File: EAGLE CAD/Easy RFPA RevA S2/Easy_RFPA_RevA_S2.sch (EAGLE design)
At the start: 197 parts, among them J101 COAX112640BNC_EDGE, J102 COAX112640BNC_EDGE, J301 COAX112640BNC_EDGE, J302 COAX112640BNC_EDGE, J401 HDR_2X1282836-1282836-1, J402 KK_PCFAN, Q101 IRF520N, Q102 IRF630, Q201 IRF630, Q202 IRF630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

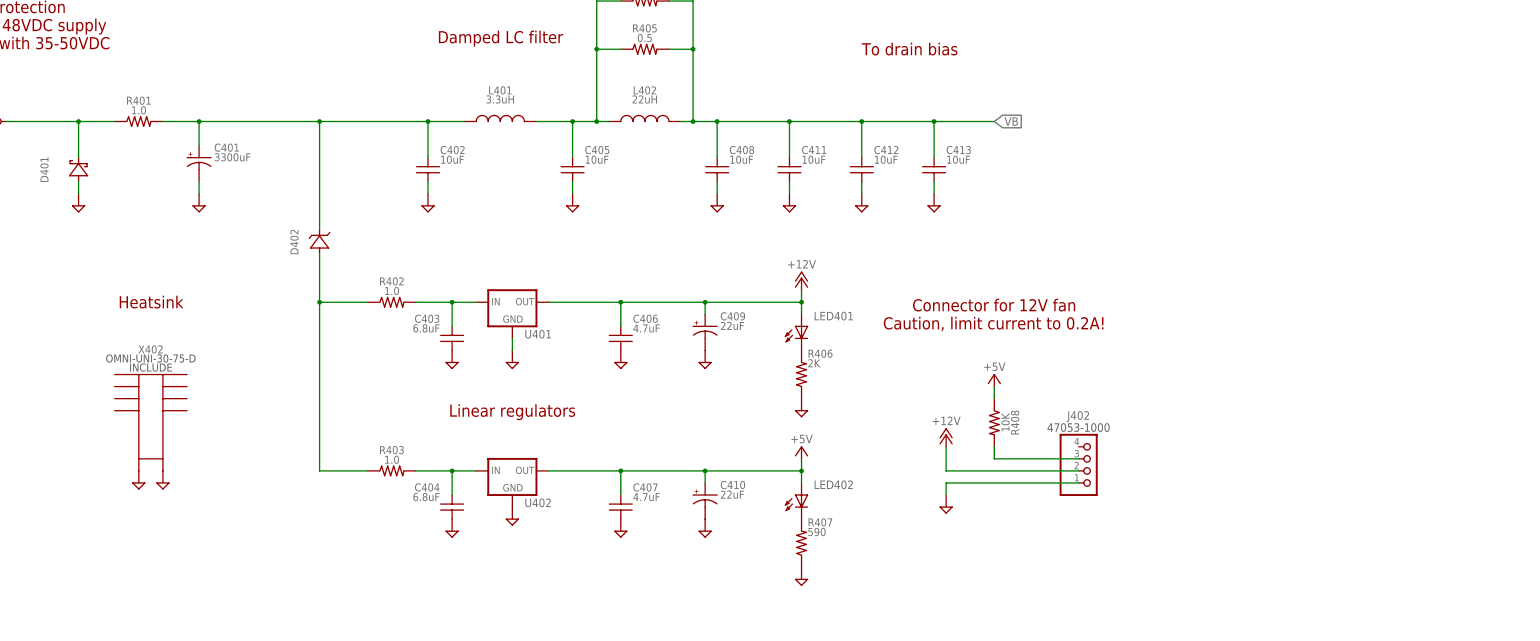
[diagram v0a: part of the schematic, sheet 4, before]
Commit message: Copy the pads and clips to revA S1 and S2
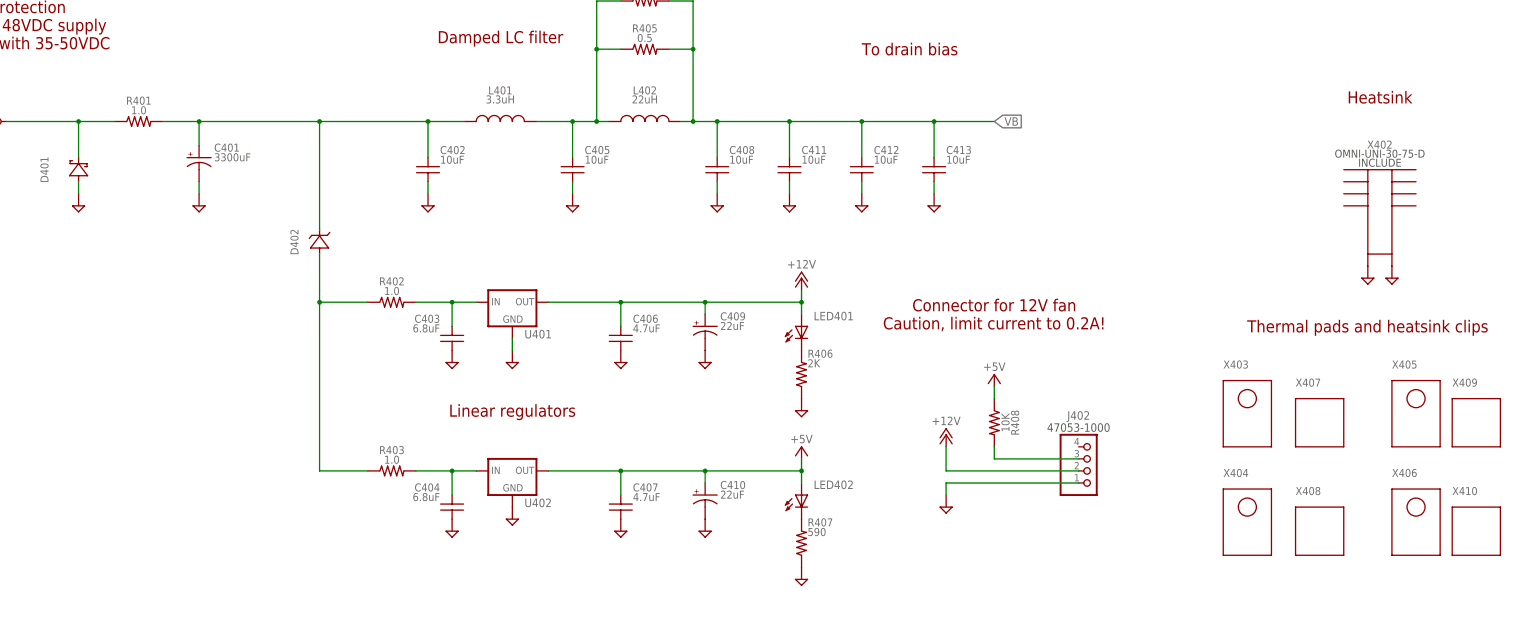
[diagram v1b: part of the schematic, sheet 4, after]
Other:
- note added: "Thermal pads and heatsink clips"
- moved on the sheet: X402
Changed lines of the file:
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@@
 </part>
 <part name="J401" library="MDT_CON" deviceset="HDR_2X1" device="282836-1" technology="282836-1"/>
+<part name="X403" library="MDT_HEATSINK" deviceset="THERMALPAD_TO220" device="" technology="DC0011/15-TI900-0.12-0"/>
+<part name="X404" library="MDT_HEATSINK" deviceset="THERMALPAD_TO220" device="" technology="DC0011/15-TI900-0.12-0"/>
+<part name="X406" library="MDT_HEATSINK" deviceset="THERMALPAD_TO220" device="" technology="DC0011/15-TI900-0.12-0"/>
+<part name="X405" library="MDT_HEATSINK" deviceset="THERMALPAD_TO220" device="" technology="DC0011/15-TI900-0.12-0"/>
+<part name="X408" library="MDT_HEATSINK" deviceset="HEATSINK_CLIP" device="" technology="OMNI-220C"/>
+<part name="X407" library="MDT_HEATSINK" deviceset="HEATSINK_CLIP" device="" technology="OMNI-220C"/>
+<part name="X409" library="MDT_HEATSINK" deviceset="HEATSINK_CLIP" device="" technology="OMNI-220C"/>
+<part name="X410" library="MDT_HEATSINK" deviceset="HEATSINK_CLIP" device="" technology="OMNI-220C"/>
 </parts>
 <sheets>
@@
 <plain>
 <text x="73.66" y="137.16" size="2.54" layer="94" align="center">Mounting holes</text>
-<text x="121.92" y="137.16" size="2.54" layer="94" align="center">Heatsink</text>
+<text x="381" y="180.34" size="2.54" layer="94" align="center">Heatsink</text>
 <text x="91.44" y="195.58" size="2.54" layer="94" align="center">Input protection
 Intended for 48VDC supply
@@
 Max duty cycle: 3.5% (500us, 70Hz rep rate, passive convection)
 Max pulse width: 1ms</text>
+<text x="378.46" y="132.08" size="2.54" layer="94" align="center">Thermal pads and heatsink clips</text>
 </plain>
 <instances>
@@
 <instance part="SUPPLY410" gate="GND" x="220.98" y="124.46" smashed="yes"/>
 <instance part="SUPPLY411" gate="GND" x="220.98" y="88.9" smashed="yes"/>
-<instance part="SUPPLY421" gate="GND" x="119.38" y="99.06" smashed="yes"/>
-<instance part="SUPPLY422" gate="GND" x="124.46" y="99.06" smashed="yes"/>
-<instance part="X402" gate="G$1" x="121.92" y="104.14"/>
+<instance part="SUPPLY421" gate="GND" x="378.46" y="142.24" smashed="yes"/>
+<instance part="SUPPLY422" gate="GND" x="383.54" y="142.24" smashed="yes"/>
+<instance part="X402" gate="G$1" x="381" y="147.32"/>
 <instance part="F401" gate="G$1" x="83.82" y="175.26" smashed="yes">
 <attribute name="NAME" x="83.82" y="180.34" size="1.778" layer="95" align="bottom-center"/>
@@
 <instance part="SUPPLY413" gate="GND" x="238.76" y="124.46" smashed="yes"/>
 <instance part="J401" gate="G$1" x="55.88" y="172.72" rot="MR0"/>
+<instance part="X403" gate="G$1" x="353.06" y="116.84"/>
+<instance part="X404" gate="G$1" x="353.06" y="93.98"/>
+<instance part="X406" gate="G$1" x="388.62" y="93.98"/>
+<instance part="X405" gate="G$1" x="388.62" y="116.84"/>
+<instance part="X408" gate="G$1" x="368.3" y="88.9"/>
+<instance part="X407" gate="G$1" x="368.3" y="111.76"/>
+<instance part="X409" gate="G$1" x="401.32" y="111.76"/>
+<instance part="X410" gate="G$1" x="401.32" y="88.9"/>
 </instances>
 <busses>

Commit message: re-export boms
one of the FETs in S1 had irf520n as the value?
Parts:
- Q101: value IRF520N -> IRF630
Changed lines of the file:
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@@
 </classes>
 <parts>
-<part name="Q101" library="MDT_TRANS" deviceset="MOSFET_N" device="TO-220-VERT" technology="IRF630" value="IRF520N"/>
+<part name="Q101" library="MDT_TRANS" deviceset="MOSFET_N" device="TO-220-VERT" technology="IRF630" value="IRF630"/>
 <part name="FRAME301" library="frames" deviceset="FRAME_B_L" device=""/>
 <part name="FRAME101" library="frames" deviceset="FRAME_B_L" device=""/>

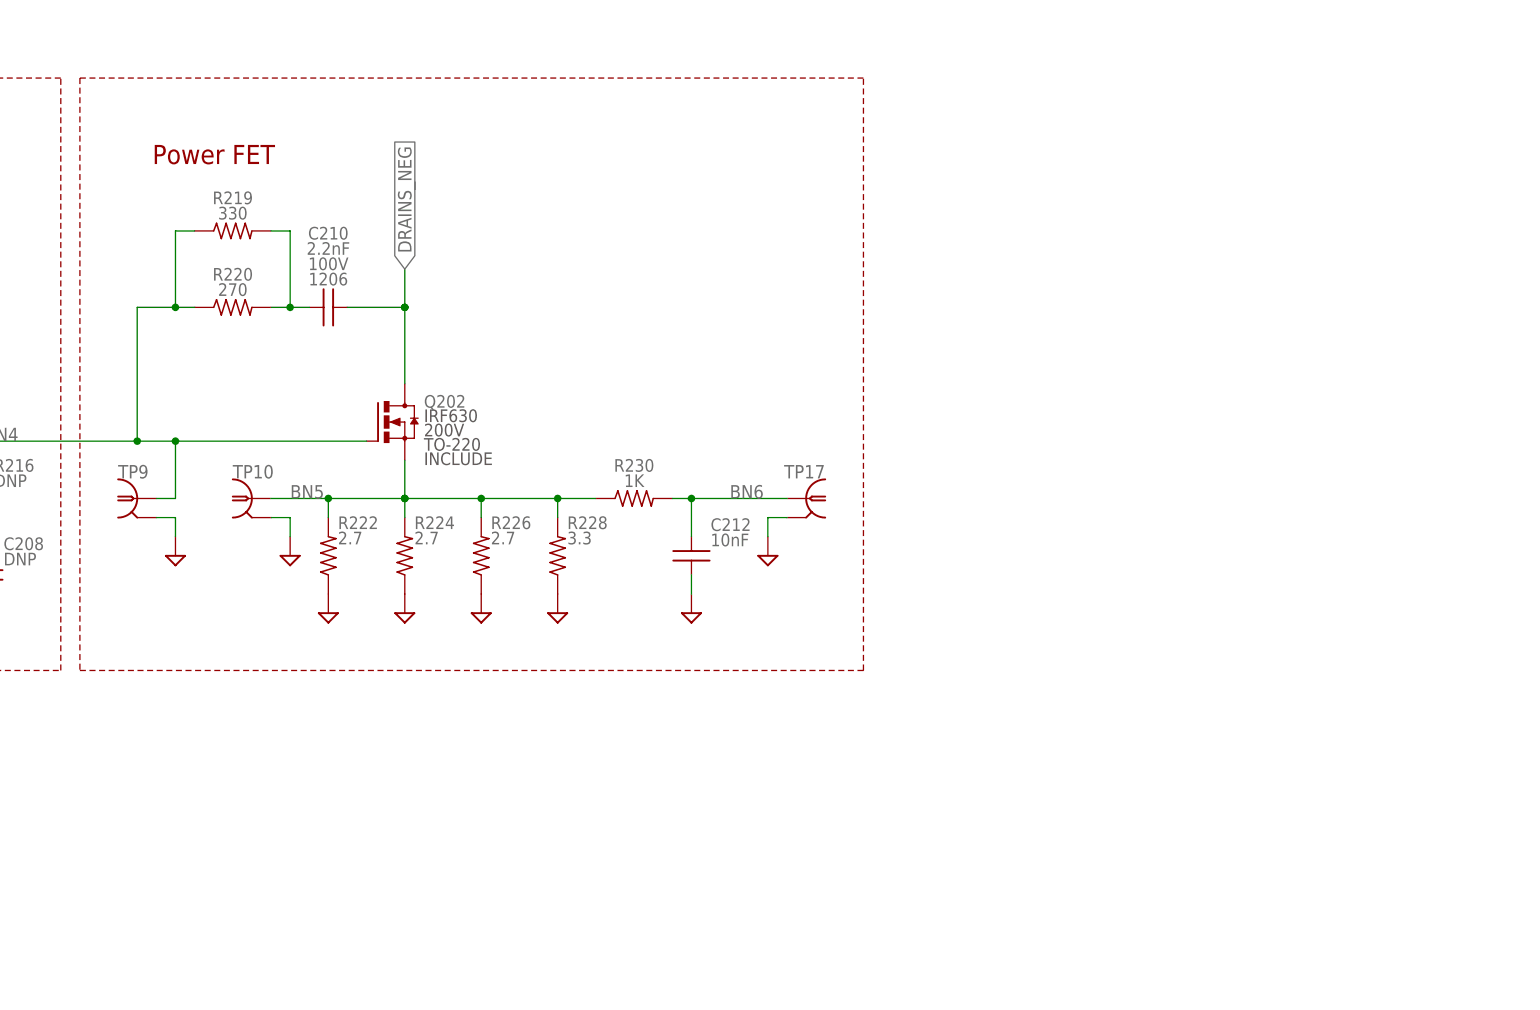
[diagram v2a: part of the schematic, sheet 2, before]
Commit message: Add global attributes and sheet names
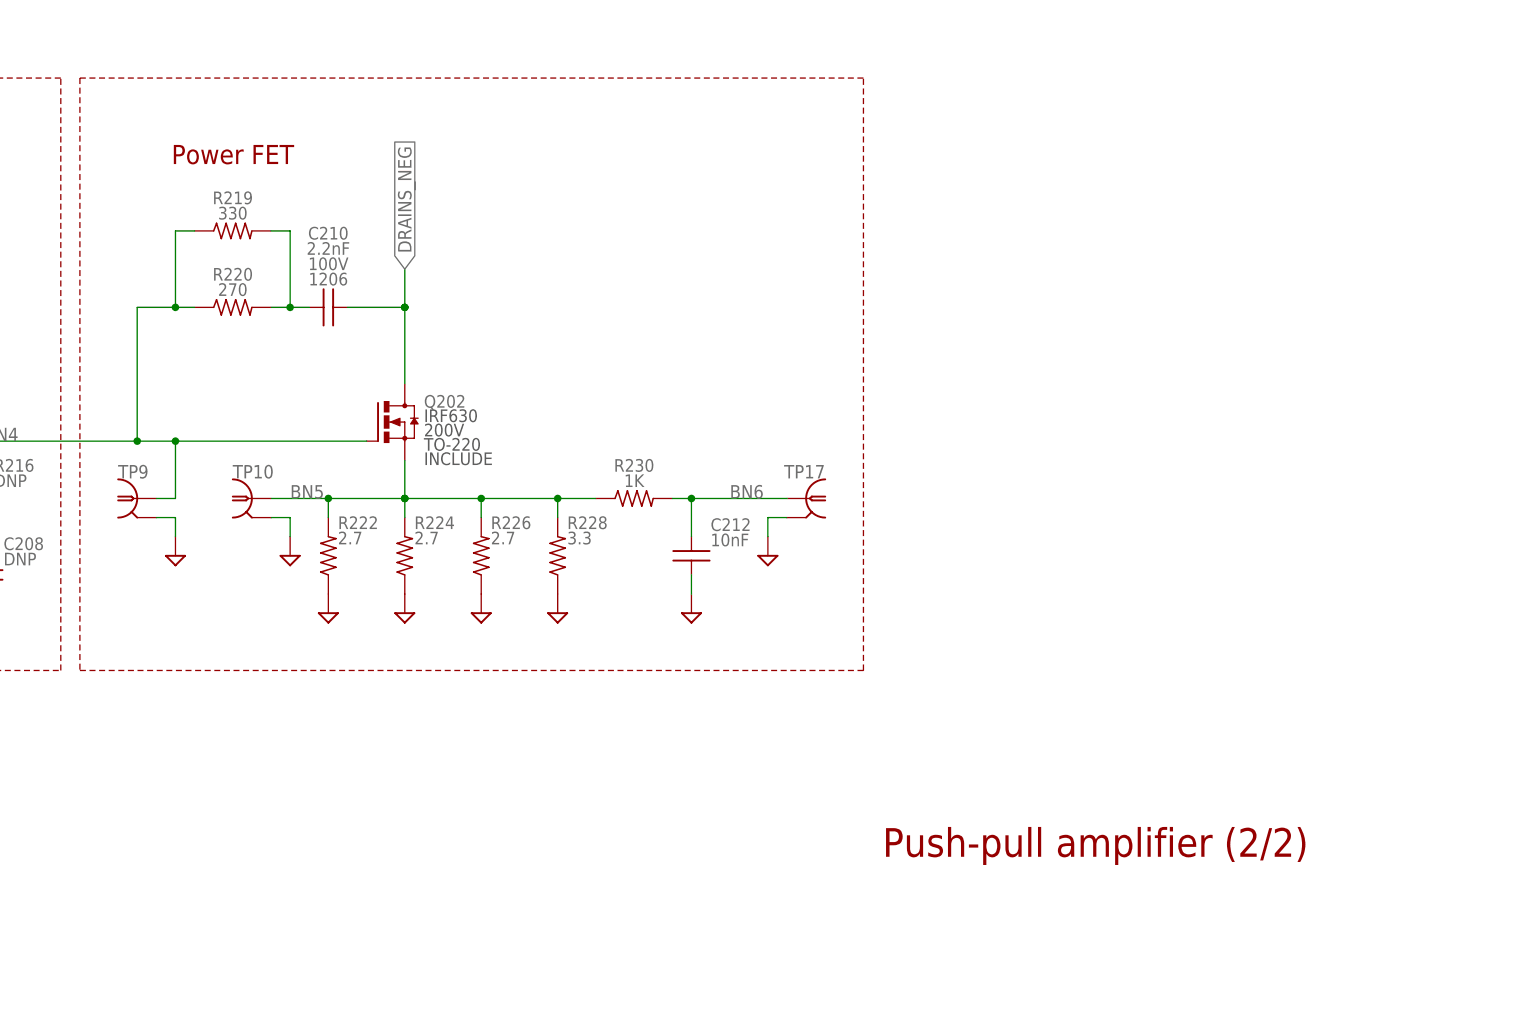
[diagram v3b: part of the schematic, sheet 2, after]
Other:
- note added: "Gate bias control"
- note added: "Power entry"
- note added: "Push-pull amplifier (1/2)"
- note added: "Push-pull amplifier (2/2)"
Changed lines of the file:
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@@
 <schematic xreflabel="%F%N" xrefpart="/%S.%C%R">
 <attributes>
+<attribute name="AUTHOR" value="MDT"/>
+<attribute name="BOMREV" value="01"/>
+<attribute name="DRAWING_NUMBER" value=" "/>
+<attribute name="FABREV" value="A"/>
 </attributes>
 <variantdefs>
@@
 Max duty cycle: 3.5% (500us, 70Hz rep rate, passive convection)
 Max pulse width: 1ms</text>
+<text x="327.66" y="27.94" size="3.81" layer="94" align="center-left">Push-pull amplifier (1/2)</text>
 </plain>
 <instances>
@@
 <text x="195.58" y="119.38" size="2.54" layer="94" align="center">Gate damping</text>
 <text x="241.3" y="218.44" size="2.54" layer="94" align="center">Power FET</text>
-<text x="238.76" y="119.38" size="2.54" layer="94" align="center">Power FET</text>
+<text x="241.3" y="119.38" size="2.54" layer="94" align="center">Power FET</text>
 <text x="7.62" y="5.08" size="3.048" layer="94">! Caution !!
 Current design lacks advanced self-protection features!
@@
 Max duty cycle: 3.5% (500us, 70Hz rep rate, passive convection)
 Max pulse width: 1ms</text>
+<text x="327.66" y="27.94" size="3.81" layer="94" align="center-left">Push-pull amplifier (2/2)</text>
 </plain>
 <instances>
@@
 Max duty cycle: 3.5% (500us, 70Hz rep rate, passive convection)
 Max pulse width: 1ms</text>
+<text x="327.66" y="27.94" size="3.81" layer="94" align="center-left">Gate bias control</text>
 </plain>
 <instances>
@@
 Max pulse width: 1ms</text>
 <text x="378.46" y="132.08" size="2.54" layer="94" align="center">Thermal pads and heatsink clips</text>
+<text x="327.66" y="27.94" size="3.81" layer="94" align="center-left">Power entry</text>
 </plain>
 <instances>
